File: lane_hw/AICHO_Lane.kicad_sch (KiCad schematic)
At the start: 53 parts, among them J1 JST PH, J2 RJ45, J41 JST PH, J42 JST PH, J43 JST PH, J9 Conn_01x04, Q41 AO3400A, Q42 AO3400A, Q43 AO3400A, U1 TPS54302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

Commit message: lane_hw: Pull-up/-down (fail-safe) resistors on EIA-485
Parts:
- added R6, R7: 2.2k, Resistor_SMD:R_0402_1005Metric, symbol Device:R
- renumbered R7 to R9
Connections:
- net +5V: now also R6.1
- net GND: now also R7.2
- net RS485_A: now also R6.2
- net RS485_B: now also R7.1

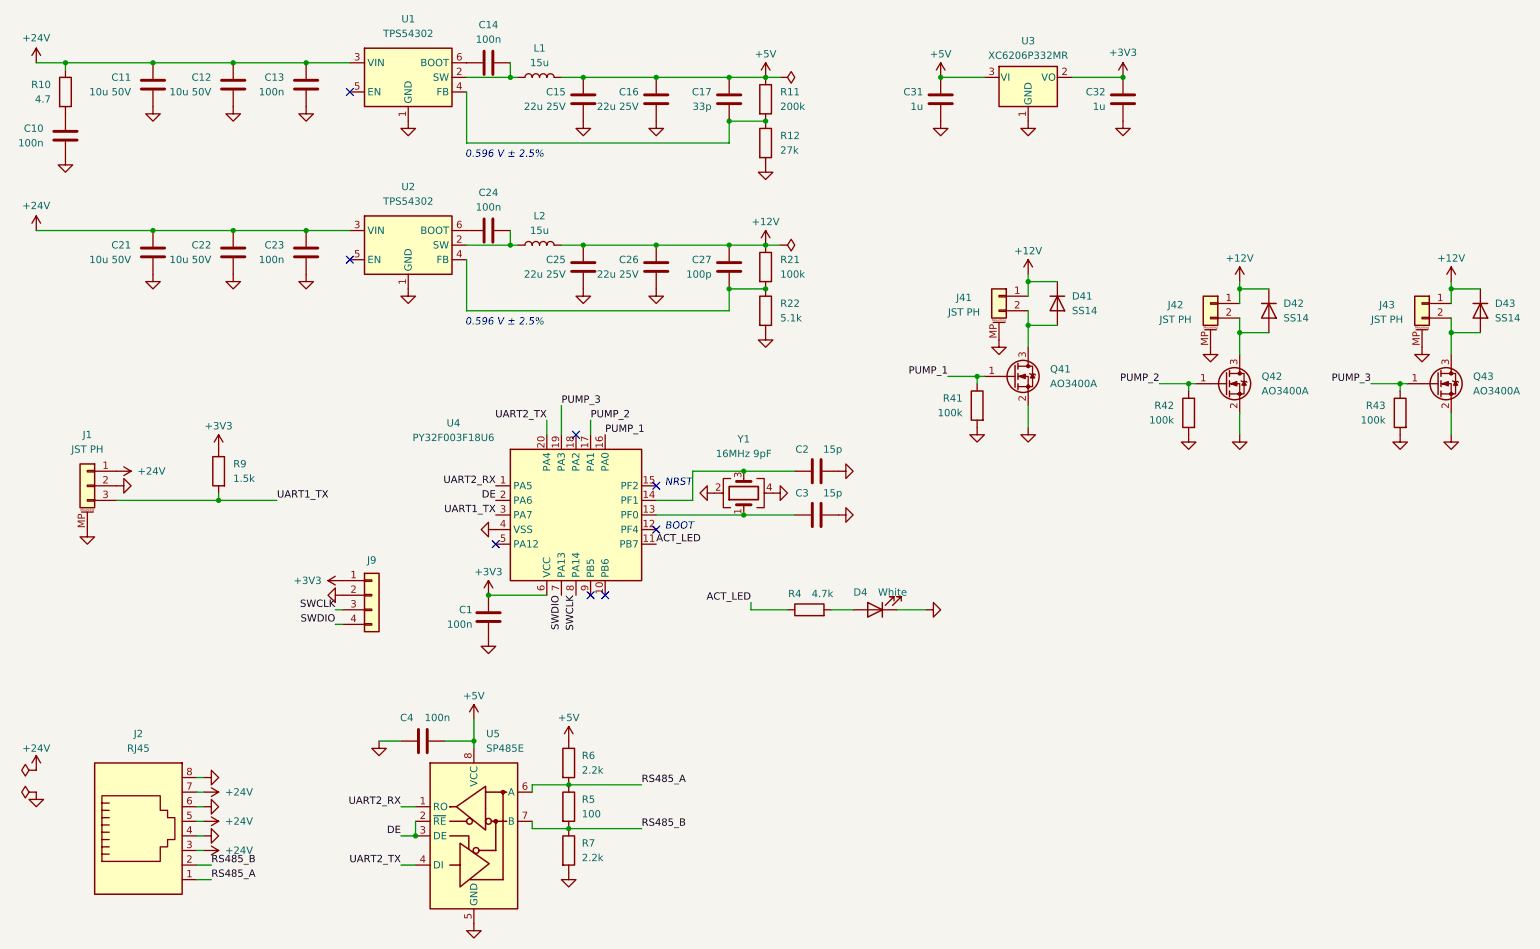
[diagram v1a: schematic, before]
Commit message: lane_hw: Revise resistors
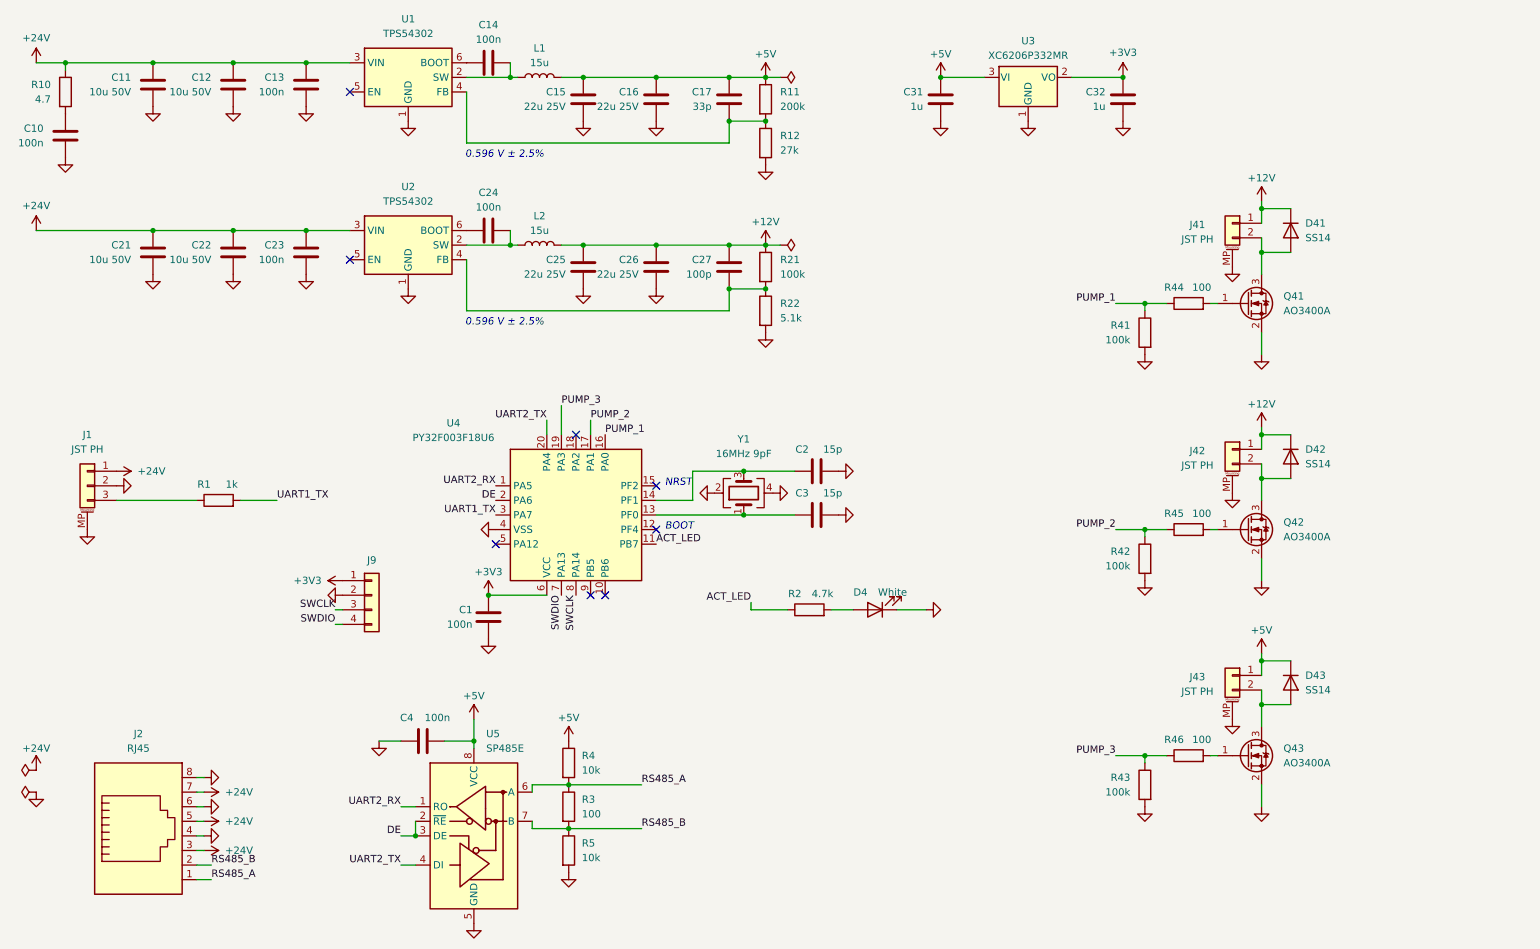
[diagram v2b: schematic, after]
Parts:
- removed R9: 1.5k, Resistor_SMD:R_0402_1005Metric, symbol Device:R
- added R1: 1k, Resistor_SMD:R_0402_1005Metric, symbol Device:R
- added R44, R45, R46: 100, Resistor_SMD:R_0402_1005Metric, symbol Device:R
- R4: renamed from R6; value 2.2k -> 10k
- R5: renamed from R7; value 2.2k -> 10k
- renumbered R4 to R2, R5 to R3
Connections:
- net +12V: no longer D43.1 (K), J43.1 (Pin_1)
- net +5V: now also D43.1 (K), J43.1 (Pin_1)
- net PUMP_1: now also R44.1; no longer Q41.1 (G)
- net PUMP_2: now also R45.1; no longer Q42.1 (G)
- net PUMP_3: now also R46.1; no longer Q43.1 (G)
- net UART1_TX: now also R1.2; no longer J1.3 (Pin_3)
- new net: Q43.1 (G), R46.2
- new net: J1.3 (Pin_3), R1.1
- new net: Q41.1 (G), R44.2
- new net: Q42.1 (G), R45.2
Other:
- moved on the sheet: D41, D42, D43, J41, J42, J43, Q41, Q42, Q43, R41, R42, R43

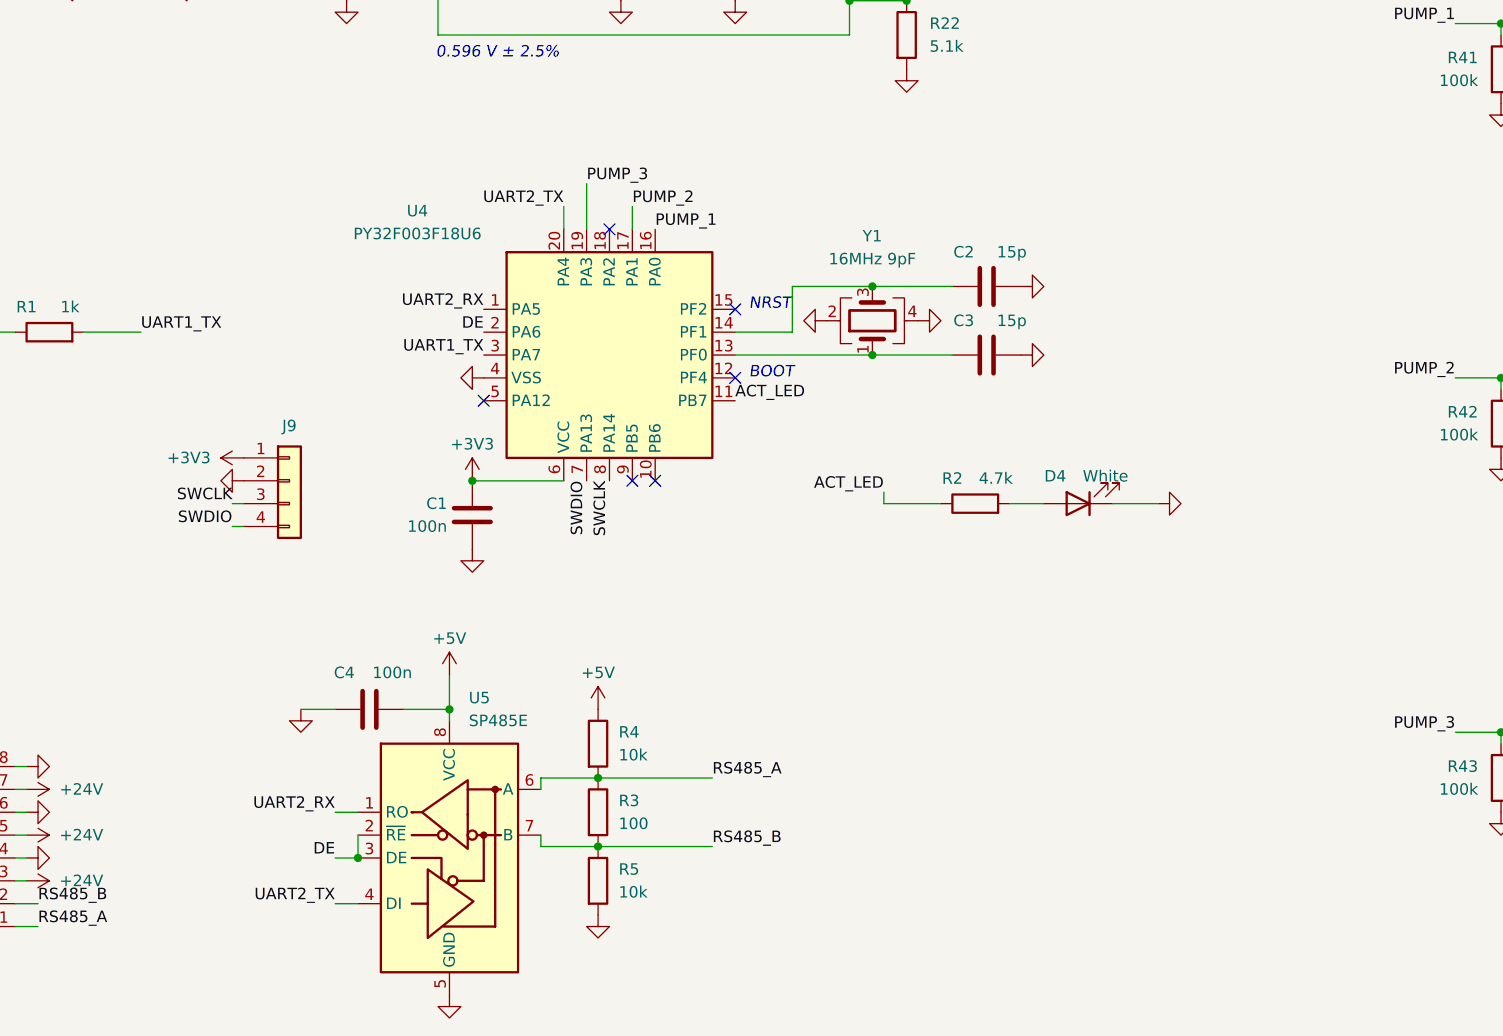
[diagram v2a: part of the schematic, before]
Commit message: lane_hw: Add pressure sensor
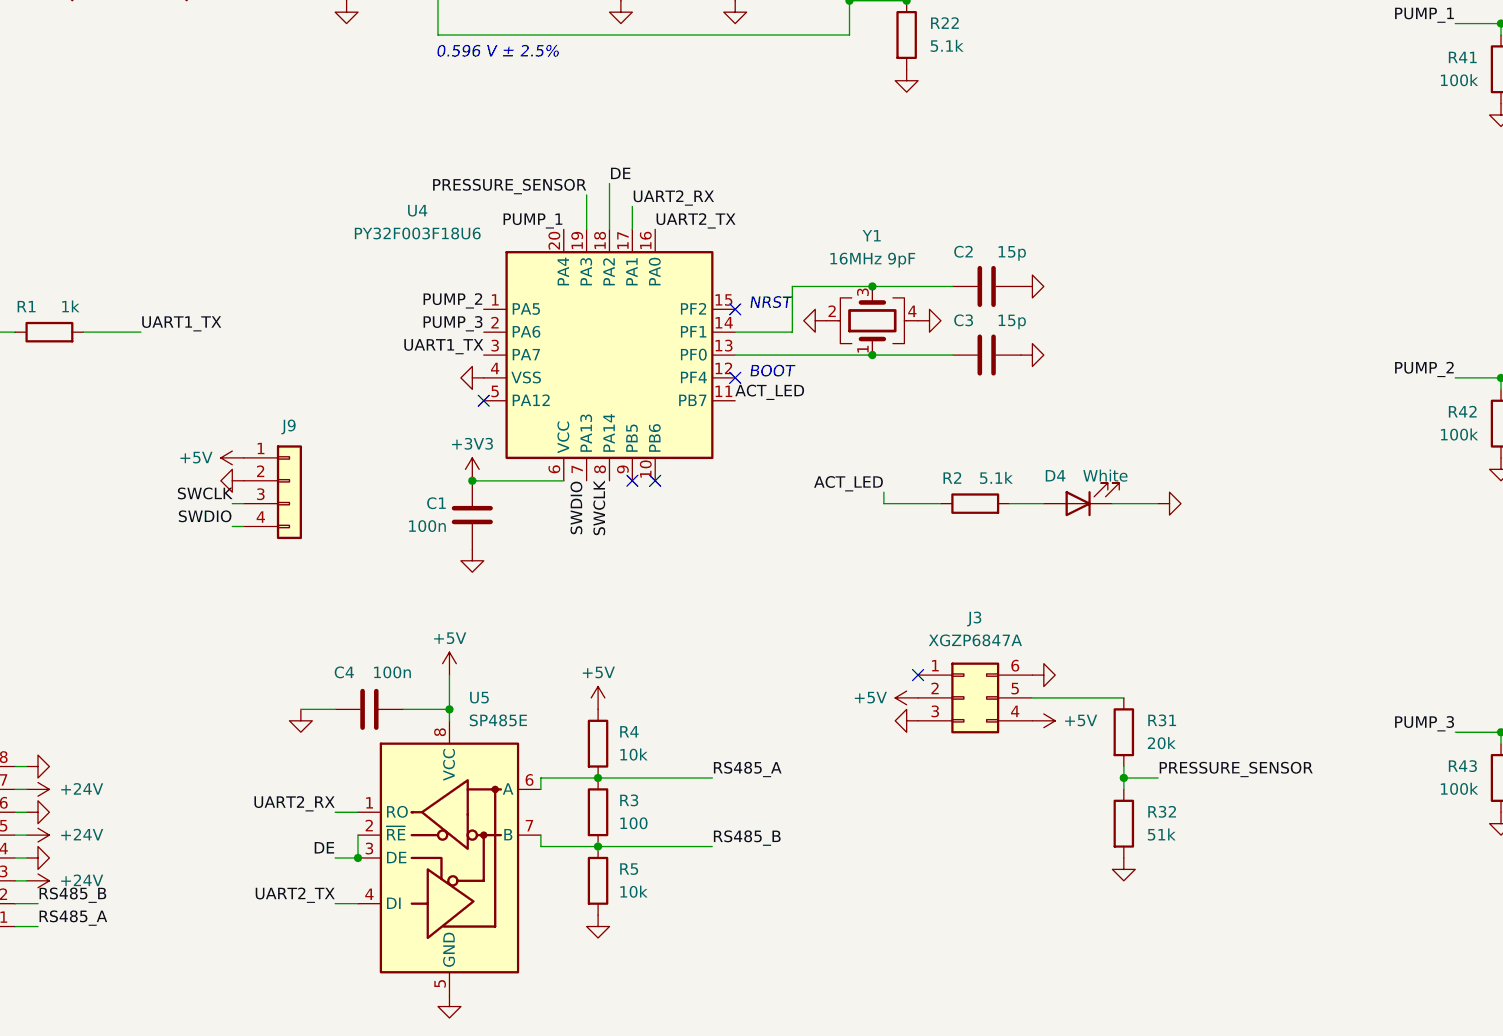
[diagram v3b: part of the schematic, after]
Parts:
- added J3: XGZP6847A, XGZP6847A:XGZP6847A, symbol Connector_Generic:Conn_02x03_Counter_Clockwise
- added R31: 20k, Resistor_SMD:R_0402_1005Metric, symbol Device:R
- added R32: 51k, Resistor_SMD:R_0402_1005Metric, symbol Device:R
- R2: value 4.7k -> 5.1k
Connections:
- net +3V3: no longer J9.1 (Pin_1)
- net +5V: now also J9.1 (Pin_1), J3.2 (Pin_2), J3.4 (Pin_4)
- net DE: now also U4.18 (PA2); no longer U4.2 (PA6)
- net GND: now also J3.3 (Pin_3), J3.6 (Pin_6), R32.2
- net PUMP_1: now also U4.20 (PA4); no longer U4.16 (PA0)
- net PUMP_2: now also U4.1 (PA5); no longer U4.17 (PA1)
- net PUMP_3: now also U4.2 (PA6); no longer U4.19 (PA3)
- net UART2_RX: now also U4.17 (PA1); no longer U4.1 (PA5)
- net UART2_TX: now also U4.16 (PA0); no longer U4.20 (PA4)
- new net: J3.5 (Pin_5), R31.1
- new net PRESSURE_SENSOR: R31.2, R32.1, U4.19 (PA3)

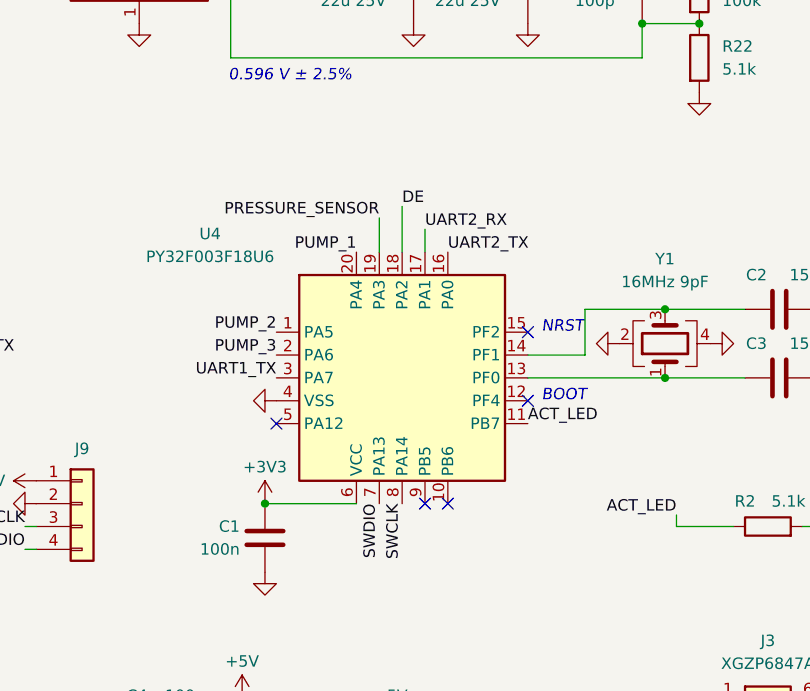
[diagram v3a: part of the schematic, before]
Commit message: lane_hw: Reassign pins
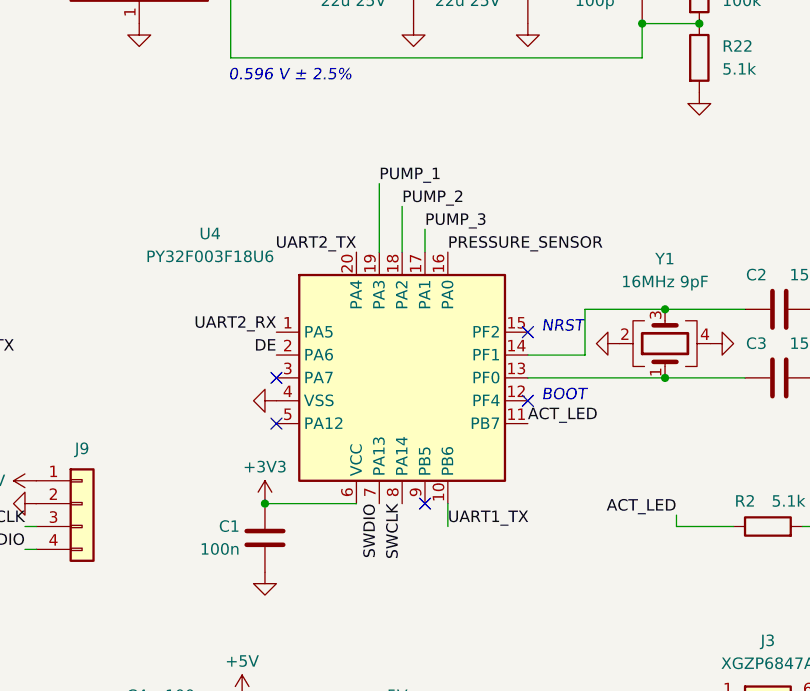
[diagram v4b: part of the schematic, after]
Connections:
- net DE: now also U4.2 (PA6); no longer U4.18 (PA2)
- net PRESSURE_SENSOR: now also U4.16 (PA0); no longer U4.19 (PA3)
- net PUMP_1: now also U4.19 (PA3); no longer U4.20 (PA4)
- net PUMP_2: now also U4.18 (PA2); no longer U4.1 (PA5)
- net PUMP_3: now also U4.17 (PA1); no longer U4.2 (PA6)
- net UART1_TX: now also U4.10 (PB6); no longer U4.3 (PA7)
- net UART2_RX: now also U4.1 (PA5); no longer U4.17 (PA1)
- net UART2_TX: now also U4.20 (PA4); no longer U4.16 (PA0)
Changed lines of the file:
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@@
-	)
-	(no_connect
-		(at 123.19 121.92)
 	)
 	(no_connect
@@
 		(at 152.4 143.51)
 	)
+	(no_connect
+		(at 104.14 107.95)
+	)
 	(wire
 		(pts
@@
 	(wire
 		(pts
+			(xy 123.19 121.92) (xy 123.19 124.46)
+		)
+		(stroke
+			(width 0)
+			(type default)
+		)
+	)
+	(wire
+		(pts
 			(xy 217.17 71.12) (xy 220.98 71.12)
 		)
@@
 	(wire
 		(pts
-			(xy 115.57 90.17) (xy 115.57 93.98)
+			(xy 115.57 86.36) (xy 115.57 93.98)
 		)
 		(stroke
@@
 		)
 	)
-	(label "PUMP_2"
+	(label "UART2_RX"
 		(at 104.14 102.87 180)
 		(effects
@@
 		)
 	)
-	(label "PRESSURE_SENSOR"
-		(at 115.57 90.17 180)
-		(effects
-			(font
-				(size 1.27 1.27)
-			)
-			(justify right bottom)
+	(label "PUMP_1"
+		(at 115.57 86.36 0)
+		(effects
+			(font
+				(size 1.27 1.27)
+			)
+			(justify left bottom)
 		)
 	)
@@
 	)
 	(label "UART1_TX"
-		(at 104.14 107.95 180)
-		(effects
-			(font
-				(size 1.27 1.27)
-			)
-			(justify right bottom)
+		(at 123.19 124.46 0)
+		(effects
+			(font
+				(size 1.27 1.27)
+			)
+			(justify left bottom)
 		)
 	)
@@
 		)
 	)
-	(label "DE"
+	(label "PUMP_2"
 		(at 118.11 88.9 0)
 		(effects
@@
 		)
 	)
+	(label "DE"
+		(at 104.14 105.41 180)
+		(effects
+			(font
+				(size 1.27 1.27)
+			)
+			(justify right bottom)
+		)
+	)
 	(label "PUMP_3"
-		(at 104.14 105.41 180)
-		(effects
-			(font
-				(size 1.27 1.27)
-			)
-			(justify right bottom)
-		)
-	)
-	(label "UART2_RX"
 		(at 120.65 91.44 0)
 		(effects
@@
 		)
 	)
-	(label "PUMP_1"
+	(label "UART2_TX"
 		(at 113.03 93.98 180)
 		(effects
@@
 		)
 	)
-	(label "UART2_TX"
+	(label "PRESSURE_SENSOR"
 		(at 123.19 93.98 0)
 		(effects

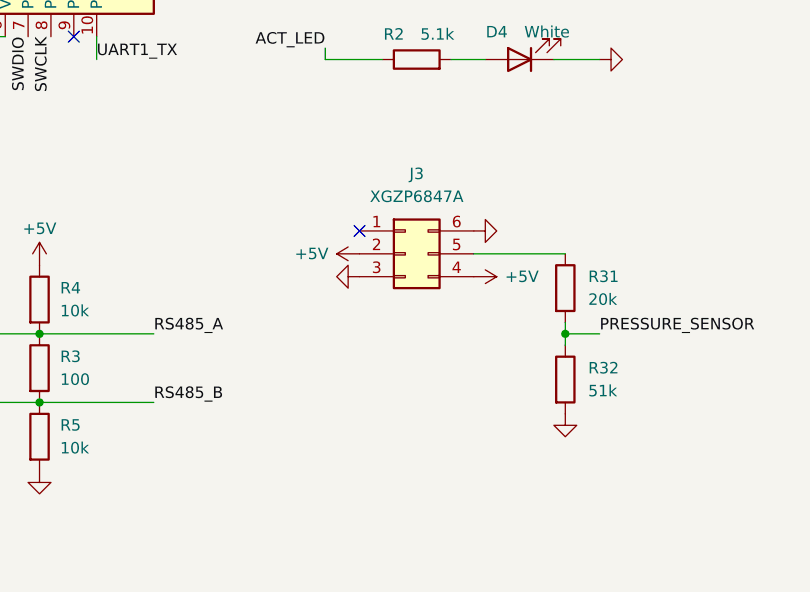
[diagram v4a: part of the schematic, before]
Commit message: lane_hw: Add capacitors around pressure sensor
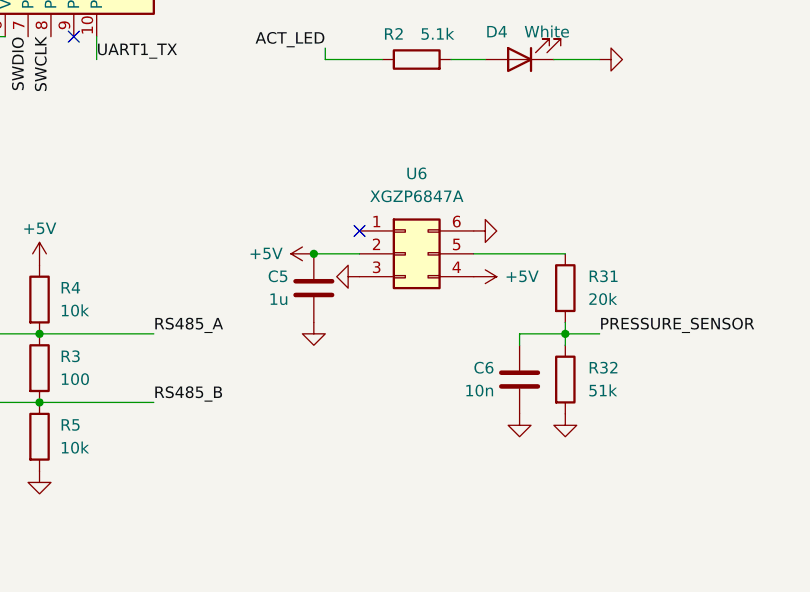
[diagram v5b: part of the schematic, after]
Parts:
- added C5: 1u, Capacitor_SMD:C_0402_1005Metric, symbol Device:C
- added C6: 10n, Capacitor_SMD:C_0402_1005Metric, symbol Device:C
- renumbered J3 to U6
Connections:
- net +5V: now also C5.1
- net GND: now also C5.2, C6.2
- net PRESSURE_SENSOR: now also C6.1
